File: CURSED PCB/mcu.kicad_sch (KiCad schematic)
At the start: 1 part, among them U3 STM32H733VGT6

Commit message: updated schematic
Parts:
- removed U3: STM32H733VGT6, stm:LQFP100_STM, symbol STM32H733VGT6:STM32H733VGT6
- added C2, C5: 6pF, Capacitor_SMD:C_0805_2012Metric_Pad1.18x1.45mm_HandSolder, symbol PCM_Capacitor_US_AKL:C_0201
- added C24: 10nF, Capacitor_SMD:C_0805_2012Metric_Pad1.18x1.45mm_HandSolder, symbol PCM_Capacitor_US_AKL:C_0201
- added C25, C26, C6: 100nF, Capacitor_SMD:C_0805_2012Metric_Pad1.18x1.45mm_HandSolder, symbol PCM_Capacitor_US_AKL:C_0201
- added C27: 4.7uF, Capacitor_SMD:C_0805_2012Metric_Pad1.18x1.45mm_HandSolder, symbol PCM_Capacitor_US_AKL:C_0201
- added C7: 1uF, Capacitor_SMD:C_0805_2012Metric_Pad1.18x1.45mm_HandSolder, symbol PCM_Capacitor_US_AKL:C_0201
- added D1: BLUE LED, LED_SMD:LED_1206_3216Metric_Pad1.42x1.75mm_HandSolder, symbol Device:LED
- added D2: RED LED, LED_SMD:LED_1206_3216Metric_Pad1.42x1.75mm_HandSolder, symbol Device:LED
- added J3: 2 Wire Block for laser, 691137710002:691137710002, symbol 691137710002:691137710002
- added JP1: Jumper, Jumper:SolderJumper-2_P1.3mm_Bridged2Bar_Pad1.0x1.5mm, symbol Jumper:Jumper_2_Small_Bridged
- added JP2: SolderJumper_2_Open, Jumper:SolderJumper-2_P1.3mm_Open_Pad1.0x1.5mm, symbol Jumper:SolderJumper_2_Open
- added R1, R2: 220R, Resistor_SMD:R_0805_2012Metric_Pad1.20x1.40mm_HandSolder, symbol Device:R_US
- added TP1: SCLK TP, TestPoint:TestPoint_Pad_1.5x1.5mm, symbol Connector:TestPoint
- added TP4: MOSI TP, TestPoint:TestPoint_Pad_1.5x1.5mm, symbol Connector:TestPoint
- added TP5: MISO TP, TestPoint:TestPoint_Pad_1.5x1.5mm, symbol Connector:TestPoint
- added U1: STM32G431KBT6, STM32G431KBT6:QFP80P900X900X160-32N, symbol STM32G431KBT6:STM32G431KBT6
- added U3: MIC94090YC6, Package_TO_SOT_SMD:SOT-363_SC-70-6, symbol Power_Management:MIC94090YC6
- added Y1: 24MHz crystal, Crystal:Crystal_SMD_Abracon_ABM8G-4Pin_3.2x2.5mm, symbol Device:Crystal_GND24
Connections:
- new net: D2.1 (K), R2.1
- new net: D1.2 (A), D2.2 (A), JP1.1 (A)
- new net: R2.2, U1.7 (PA2)
- new net: R1.2, U1.8 (PA3)
- new net: D1.1 (K), R1.1
- new net: J3.2, JP2.1 (A)
- new net: JP2.2 (B), U3.1 (OUT)
- new net +3.3VA: C24.2, C6.1, C7.2, U1.15 (VDDA/VREF+)
- new net +3.3VD: C25.2, C26.2, C27.2, JP1.2 (B), U1.1 (VDD), U1.17 (VDD)
- new net +5V: U3.4 (IN)
- new net CS2: U1.25 (PA15)
- new net CS_DAC: U1.13 (PB0)
- new net CUR_SEN: U1.5 (PA0)
- new net GND: C2.2, C24.1, C25.1, C26.1, C27.1, C5.2, C6.2, C7.1, J3.1, U1.14 (VSSA), U1.16 (VSS), U1.31 (PB8-BOOT0), U1.32 (VSS), U3.2 (GND), U3.5 (GND), Y1.2, Y1.4
- new net IRQ/MDAT: U1.6 (PA1)
- new net Las_enable: U1.30 (PB7), U3.6 (EN)
- new net MCLR: U1.4 (PG10-NRST)
- new net MISO: TP5.1, U1.11 (PA6)
- new net MKLKIN: U1.21 (PA11)
- new net MOSI: TP4.1, U1.12 (PA7)
- new net OCS1/CLKIN: C5.1, U1.2 (PF0-OSC_IN), Y1.3
- new net OCS2/CLKOUT: C2.1, U1.3 (PF1-OSC_OUT), Y1.1
- new net PGC: U1.23 (PA13)
- new net PGD: U1.24 (PA14)
- new net RXD: U1.20 (PA10)
- new net SCLK: TP1.1, U1.10 (PA5)
- new net TXD: U1.19 (PA9)
- no-connect marks 0 -> 6
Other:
- note added: "C5=C6=2*(C_L - C_S) C_L = 8 C_S = 5 C5=C6=6"

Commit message: updated schematic
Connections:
- net CS: now also U1.9 (PA4)
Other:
- note added: "Laser: https://www.iadiy.com/infrared-laser-module-LM9IR830H200D&path=168_173"
- moved on the sheet: C27, C7
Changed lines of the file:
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@@
 	(generator_version "9.0")
 	(paper "A4")
-	(text "C5=C6=2*(C_L - C_S)\n\nC_L = 8 \nC_S = 5\n\nC5=C6=6"
+	(text "Laser: https://www.iadiy.com/infrared-laser-module-LM9IR830H200D&path=168_173"
 		(exclude_from_sim no)
-		(at 31.75 151.13 0)
+		(at 225.298 159.512 0)
 		(effects
 			(font
@@
 		)
 	)
-	(junction
-		(at 191.77 58.42)
-		(diameter 0)
-		(color 0 0 0 0)
+	(text "C5=C6=2*(C_L - C_S)\n\nC_L = 8 \nC_S = 5\n\nC5=C6=6"
+		(exclude_from_sim no)
+		(at 37.338 137.414 0)
+		(effects
+			(font
+				(size 1.27 1.27)
+			)
+		)
 	)
 	(junction
@@
 	)
 	(junction
-		(at 189.23 58.42)
-		(diameter 0)
-		(color 0 0 0 0)
-	)
-	(junction
-		(at 191.77 49.53)
+		(at 193.04 49.53)
 		(diameter 0)
 		(color 0 0 0 0)
@@
 	)
 	(junction
-		(at 227.33 54.61)
+		(at 193.04 58.42)
 		(diameter 0)
 		(color 0 0 0 0)
 	)
 	(junction
-		(at 231.14 54.61)
+		(at 227.33 54.61)
 		(diameter 0)
 		(color 0 0 0 0)
@@
 	(wire
 		(pts
-			(xy 191.77 50.8) (xy 191.77 49.53)
+			(xy 193.04 50.8) (xy 193.04 49.53)
 		)
 		(stroke
@@
 	(wire
 		(pts
-			(xy 227.33 46.99) (xy 234.95 46.99)
+			(xy 193.04 58.42) (xy 200.66 58.42)
 		)
 		(stroke
@@
 	(wire
 		(pts
-			(xy 222.25 144.78) (xy 222.25 148.59)
+			(xy 227.33 46.99) (xy 233.68 46.99)
 		)
 		(stroke
@@
 	(wire
 		(pts
-			(xy 39.37 59.69) (xy 39.37 62.23)
+			(xy 222.25 144.78) (xy 222.25 148.59)
 		)
 		(stroke
@@
 	(wire
 		(pts
-			(xy 191.77 58.42) (xy 189.23 58.42)
+			(xy 39.37 59.69) (xy 39.37 62.23)
 		)
 		(stroke
@@
 	(wire
 		(pts
-			(xy 200.66 49.53) (xy 191.77 49.53)
+			(xy 200.66 49.53) (xy 193.04 49.53)
 		)
 		(stroke
@@
 	(wire
 		(pts
-			(xy 191.77 58.42) (xy 200.66 58.42)
-		)
-		(stroke
-			(width 0)
-			(type default)
-		)
-	)
-	(wire
-		(pts
 			(xy 91.44 85.09) (xy 109.22 85.09)
 		)
@@
 	(wire
 		(pts
-			(xy 189.23 58.42) (xy 189.23 62.23)
+			(xy 193.04 58.42) (xy 193.04 62.23)
 		)
 		(stroke
@@
 	(wire
 		(pts
-			(xy 231.14 54.61) (xy 234.95 54.61)
-		)
-		(stroke
-			(width 0)
-			(type default)
-		)
-	)
-	(wire
-		(pts
 			(xy 220.98 46.99) (xy 227.33 46.99)
 		)
@@
 	(wire
 		(pts
-			(xy 227.33 54.61) (xy 231.14 54.61)
+			(xy 227.33 54.61) (xy 233.68 54.61)
 		)
 		(stroke
@@
 	(wire
 		(pts
-			(xy 92.71 72.39) (xy 109.22 72.39)
+			(xy 77.47 74.93) (xy 85.09 74.93)
 		)
 		(stroke
@@
 	(wire
 		(pts
-			(xy 77.47 74.93) (xy 85.09 74.93)
+			(xy 71.12 137.16) (xy 71.12 142.24)
 		)
 		(stroke
@@
 	(wire
 		(pts
-			(xy 71.12 137.16) (xy 71.12 142.24)
+			(xy 91.44 72.39) (xy 109.22 72.39)
 		)
 		(stroke
@@
 	(wire
 		(pts
-			(xy 191.77 49.53) (xy 185.42 49.53)
+			(xy 185.42 49.53) (xy 193.04 49.53)
 		)
 		(stroke
@@
 	(wire
 		(pts
-			(xy 189.23 58.42) (xy 185.42 58.42)
+			(xy 185.42 58.42) (xy 193.04 58.42)
 		)
 		(stroke
@@
 	(wire
 		(pts
-			(xy 231.14 54.61) (xy 231.14 57.15)
+			(xy 227.33 54.61) (xy 227.33 57.15)
 		)
 		(stroke
@@
 	(symbol
 		(lib_id "PCM_Capacitor_US_AKL:C_0201")
-		(at 191.77 54.61 180)
+		(at 193.04 54.61 180)
 		(unit 1)
 		(exclude_from_sim no)
@@
 		(dnp no)
 		(property "Reference" "C7"
-			(at 194.818 53.34 0)
+			(at 196.088 53.34 0)
 			(effects
 				(font
@@
 		)
 		(property "Value" "1uF"
-			(at 194.818 55.88 0)
+			(at 196.088 55.88 0)
 			(effects
 				(font
@@
 		)
 		(property "Footprint" "Capacitor_SMD:C_0805_2012Metric_Pad1.18x1.45mm_HandSolder"
-			(at 190.8048 50.8 0)
+			(at 192.0748 50.8 0)
 			(effects
 				(font
@@
 		)
 		(property "Datasheet" "~"
-			(at 191.77 54.61 0)
+			(at 193.04 54.61 0)
 			(effects
 				(font
@@
 		)
 		(property "Description" "SMD 0201 MLCC capacitor, Alternate KiCad Library"
-			(at 191.77 54.61 0)
+			(at 193.04 54.61 0)
 			(effects
 				(font
@@
 	(symbol
 		(lib_id "power:GND")
-		(at 231.14 57.15 0)
+		(at 227.33 57.15 0)
 		(unit 1)
 		(exclude_from_sim no)
@@
 		(dnp no)
 		(property "Reference" "#PWR071"
-			(at 231.14 63.5 0)
+			(at 227.33 63.5 0)
 			(effects
 				(font
@@
 		)
 		(property "Value" "GND"
-			(at 231.1401 60.96 90)
+			(at 227.3301 60.96 90)
 			(effects
 				(font
@@
 		)
 		(property "Footprint" ""
-			(at 231.14 57.15 0)
+			(at 227.33 57.15 0)
 			(effects
 				(font
@@
 		)
 		(property "Datasheet" ""
-			(at 231.14 57.15 0)
+			(at 227.33 57.15 0)
 			(effects
 				(font
@@
 		)
 		(property "Description" "Power symbol creates a global label with name \"GND\" , ground"
-			(at 231.14 57.15 0)
+			(at 227.33 57.15 0)
 			(effects
 				(font
@@
 	(symbol
 		(lib_id "power:GND")
-		(at 189.23 62.23 0)
+		(at 193.04 62.23 0)
 		(unit 1)
 		(exclude_from_sim no)
@@
 		(dnp no)
 		(property "Reference" "#PWR068"
-			(at 189.23 68.58 0)
+			(at 193.04 68.58 0)
 			(effects
 				(font
@@
 		)
 		(property "Value" "GND"
-			(at 189.2301 66.04 90)
+			(at 193.0401 66.04 90)
 			(effects
 				(font
@@
 		)
 		(property "Footprint" ""
-			(at 189.23 62.23 0)
+			(at 193.04 62.23 0)
 			(effects
 				(font
@@
 		)
 		(property "Datasheet" ""
-			(at 189.23 62.23 0)
+			(at 193.04 62.23 0)
 			(effects
 				(font
@@
 		)
 		(property "Description" "Power symbol creates a global label with name \"GND\" , ground"
-			(at 189.23 62.23 0)
+			(at 193.04 62.23 0)
 			(effects
 				(font
@@
 	(symbol
 		(lib_id "PCM_Capacitor_US_AKL:C_0201")
-		(at 234.95 50.8 180)
+		(at 233.68 50.8 180)
 		(unit 1)
 		(exclude_from_sim no)
@@
 		(fields_autoplaced yes)
 		(property "Reference" "C27"
-			(at 238.76 49.5299 0)
+			(at 237.49 49.5299 0)
 			(effects
 				(font
@@
 		)
 		(property "Value" "4.7uF"
-			(at 238.76 52.0699 0)
+			(at 237.49 52.0699 0)
 			(effects
 				(font
@@
 		)
 		(property "Footprint" "Capacitor_SMD:C_0805_2012Metric_Pad1.18x1.45mm_HandSolder"
-			(at 233.9848 46.99 0)
+			(at 232.7148 46.99 0)
 			(effects
 				(font
@@
 		)
 		(property "Datasheet" "~"
-			(at 234.95 50.8 0)
+			(at 233.68 50.8 0)
 			(effects
 				(font
@@
 		)
 		(property "Description" "SMD 0201 MLCC capacitor, Alternate KiCad Library"
-			(at 234.95 50.8 0)
+			(at 233.68 50.8 0)
 			(effects
 				(font

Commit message: schematic changes
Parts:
- removed J3: 2 Wire Block for laser, 691137710002:691137710002, symbol 691137710002:691137710002
- added C35: 1uF, Capacitor_SMD:C_0805_2012Metric_Pad1.18x1.45mm_HandSolder, symbol PCM_Capacitor_US_AKL:C_0201
- added R15: 10K, Resistor_SMD:R_0805_2012Metric_Pad1.20x1.40mm_HandSolder, symbol Device:R_US
- renumbered TP5 to MITP1, TP4 to MOTP1, TP1 to SCTP1
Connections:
- net GND: now also C35.1, R15.1, R15.2
- net MCLR: now also C35.2
- net LASER: now reaches JP2.1 (A)

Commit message: schematic and layout changes
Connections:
- net DAC_RESET: now also U1.27 (PB4)
- no-connect marks 6 -> 5
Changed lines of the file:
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@@
 	)
 	(no_connect
-		(at 149.86 67.31)
-	)
-	(no_connect
 		(at 149.86 64.77)
 	)
@@
 	(wire
 		(pts
+			(xy 77.47 90.17) (xy 109.22 90.17)
+		)
+		(stroke
+			(width 0)
+			(type default)
+		)
+	)
+	(wire
+		(pts
 			(xy 74.93 137.16) (xy 71.12 137.16)
 		)
@@
 	(wire
 		(pts
-			(xy 91.44 85.09) (xy 109.22 85.09)
+			(xy 77.47 85.09) (xy 109.22 85.09)
 		)
 		(stroke
@@
 	(wire
 		(pts
-			(xy 91.44 87.63) (xy 109.22 87.63)
+			(xy 77.47 87.63) (xy 109.22 87.63)
 		)
 		(stroke
@@
 	(wire
 		(pts
-			(xy 88.9 97.79) (xy 109.22 97.79)
+			(xy 77.47 97.79) (xy 109.22 97.79)
 		)
 		(stroke
@@
 	(wire
 		(pts
-			(xy 88.9 100.33) (xy 109.22 100.33)
+			(xy 77.47 100.33) (xy 109.22 100.33)
 		)
 		(stroke
@@
 	(wire
 		(pts
-			(xy 91.44 90.17) (xy 109.22 90.17)
-		)
-		(stroke
-			(width 0)
-			(type default)
-		)
-	)
-	(wire
-		(pts
 			(xy 200.66 50.8) (xy 200.66 49.53)
 		)
@@
 	(wire
 		(pts
+			(xy 149.86 67.31) (xy 161.29 67.31)
+		)
+		(stroke
+			(width 0)
+			(type default)
+		)
+	)
+	(wire
+		(pts
 			(xy 81.28 64.77) (xy 109.22 64.77)
 		)
@@
 	(wire
 		(pts
-			(xy 88.9 95.25) (xy 109.22 95.25)
+			(xy 77.47 95.25) (xy 109.22 95.25)
 		)
 		(stroke
@@
 	(hierarchical_label "CS2"
 		(shape input)
-		(at 88.9 100.33 180)
+		(at 77.47 100.33 180)
 		(effects
 			(font
@@
 	(hierarchical_label "TXD"
 		(shape input)
-		(at 91.44 85.09 180)
+		(at 77.47 85.09 180)
 		(effects
 			(font
@@
 	(hierarchical_label "RXD"
 		(shape input)
-		(at 91.44 87.63 180)
+		(at 77.47 87.63 180)
 		(effects
 			(font
@@
 	(hierarchical_label "DAC_RESET"
 		(shape input)
-		(at 162.56 66.04 0)
+		(at 161.29 67.31 0)
 		(effects
 			(font
@@
 	(hierarchical_label "MKLKIN"
 		(shape input)
-		(at 91.44 90.17 180)
+		(at 77.47 90.17 180)
 		(effects
 			(font
@@
 	(hierarchical_label "PGC"
 		(shape input)
-		(at 88.9 95.25 180)
+		(at 77.47 95.25 180)
 		(effects
 			(font
@@
 	(hierarchical_label "PGD"
 		(shape input)
-		(at 88.9 97.79 180)
+		(at 77.47 97.79 180)
 		(effects
 			(font
@@
 		(dnp no)
 		(property "Reference" "MOTP1"
-			(at 83.058 80.772 0)
+			(at 64.008 80.518 0)
 			(effects
 				(font
@@
 		)
 		(property "Value" "MOSI TP"
-			(at 83.058 83.312 0)
+			(at 55.372 80.772 0)
 			(effects
 				(font
@@
 		(dnp no)
 		(property "Reference" "SCTP1"
-			(at 74.422 67.818 0)
+			(at 62.992 73.152 0)
 			(effects
 				(font
@@
 		)
 		(property "Value" "SCLK TP"
-			(at 74.422 70.358 0)
+			(at 53.34 73.152 0)
 			(effects
 				(font
@@
 		(dnp no)
 		(property "Reference" "MITP1"
-			(at 99.06 70.358 0)
+			(at 63.5 77.724 0)
 			(effects
 				(font
@@
 		)
 		(property "Value" "MISO TP"
-			(at 99.06 72.898 0)
+			(at 55.626 77.724 0)
 			(effects
 				(font

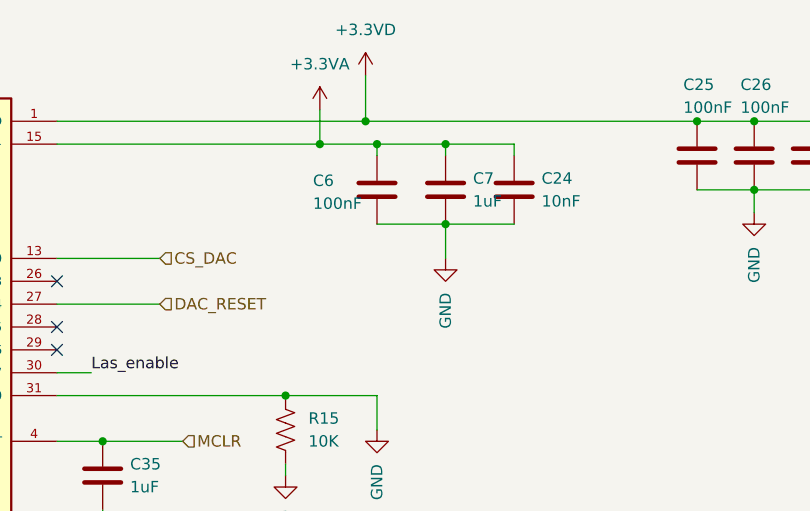
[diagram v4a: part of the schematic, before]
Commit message: updates traces and footprints
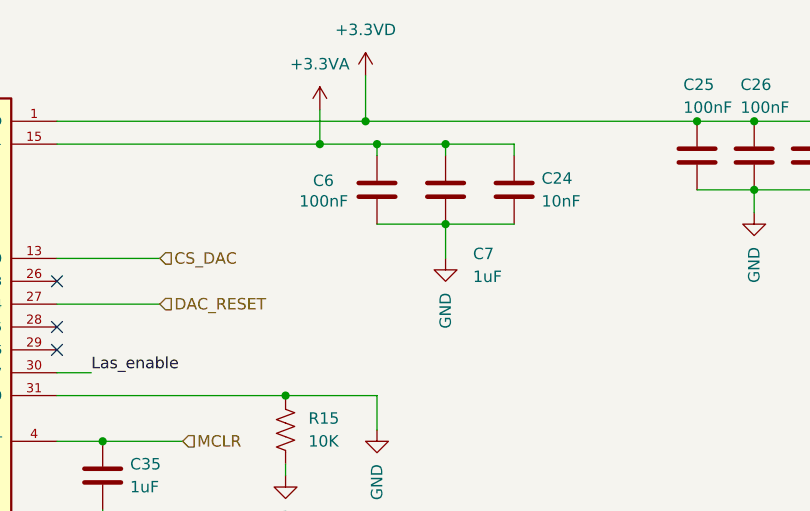
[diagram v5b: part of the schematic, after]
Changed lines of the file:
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@@
 		(dnp no)
 		(property "Reference" "C7"
-			(at 196.088 53.34 0)
+			(at 196.088 61.722 0)
 			(effects
 				(font
@@
 		)
 		(property "Value" "1uF"
-			(at 196.088 55.88 0)
+			(at 196.088 64.262 0)
 			(effects
 				(font
@@
 		)
 		(property "Value" "100nF"
-			(at 178.308 56.134 0)
-			(effects
-				(font
+			(at 176.784 55.88 0)
+			(effects
+				(font

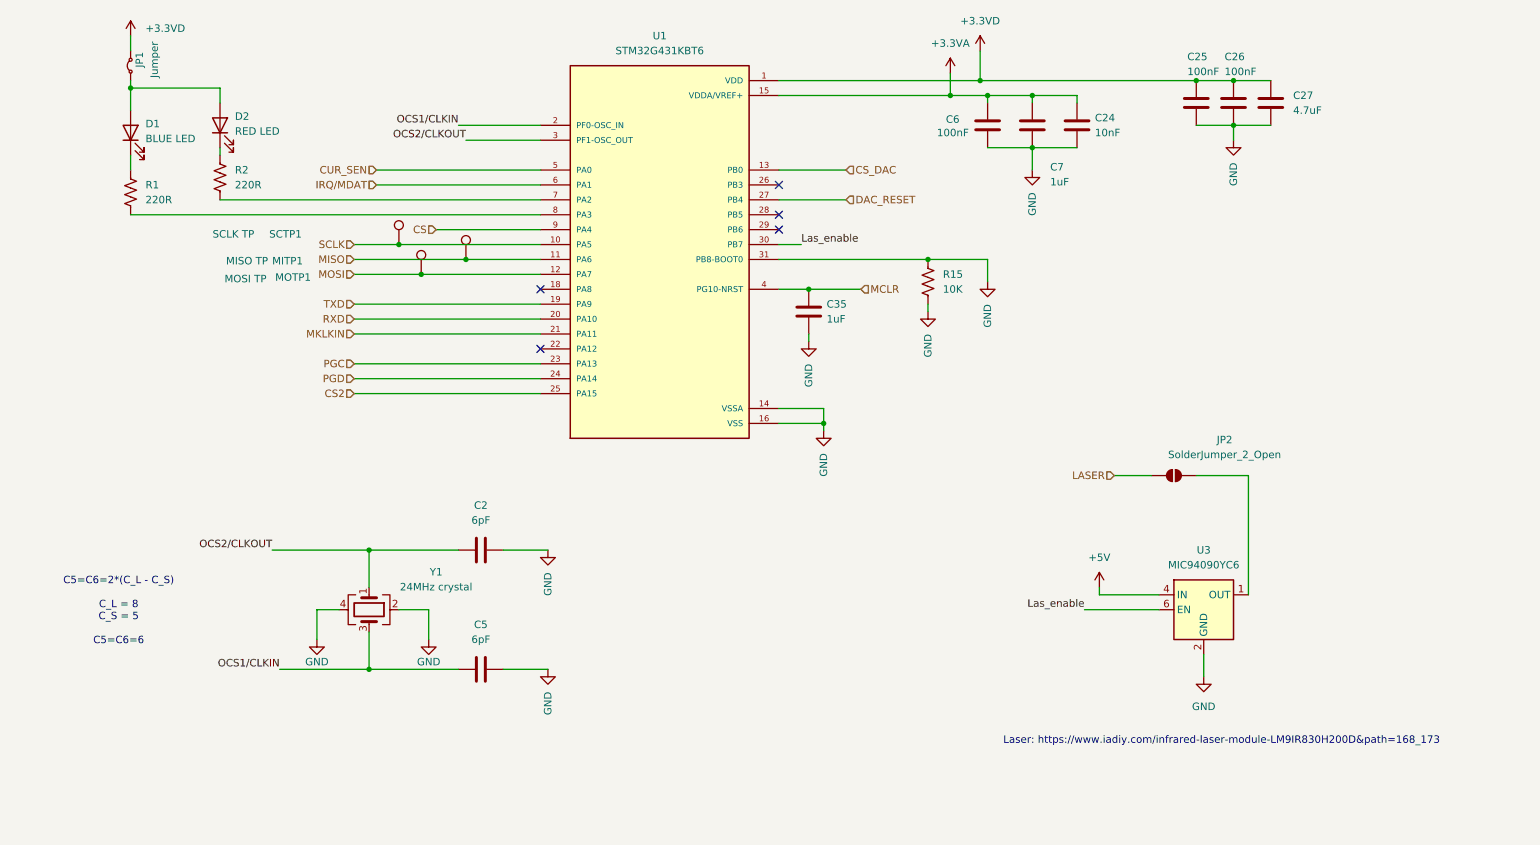
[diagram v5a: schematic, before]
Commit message: Updated PDF and make schematic look more pretty
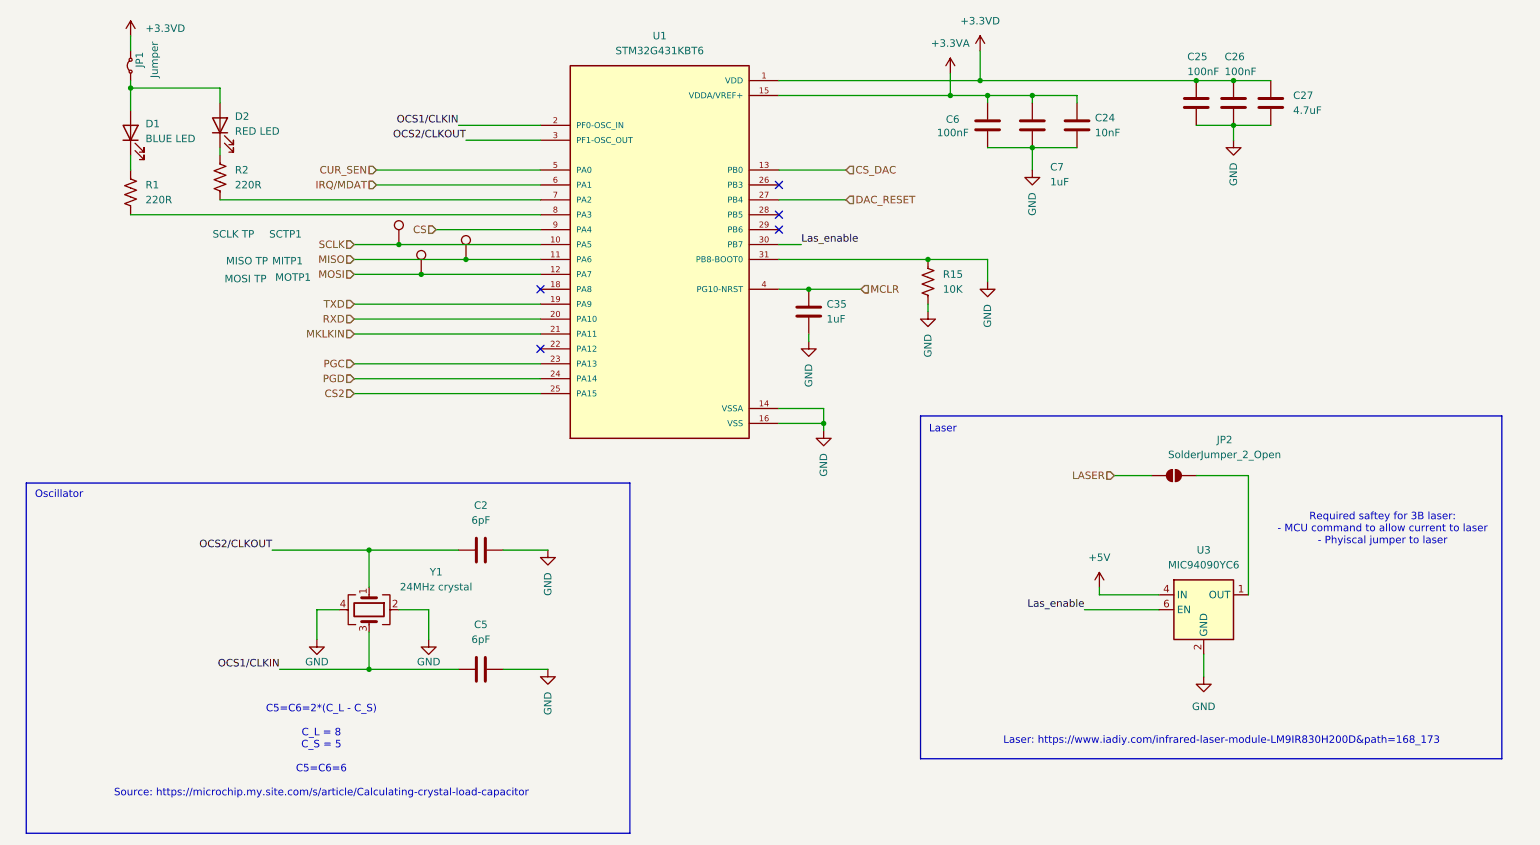
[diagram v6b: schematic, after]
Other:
- note added: "C5=C6=2*(C_L - C_S) C_L = 8 C_S = 5 C5=C6=6 Source: https://microchip.my.site.com/s/article/Calculating-crystal-load-capacitor"
- note added: "Laser"
- note added: "Oscillator"
- note added: "Required saftey for 3B laser: - MCU command to allow current to laser - Phyiscal jumper to laser"
- note removed: "C5=C6=2*(C_L - C_S) C_L = 8 C_S = 5 C5=C6=6"
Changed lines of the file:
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@@
 	(generator_version "9.0")
 	(paper "A4")
+	(rectangle
+		(start 173.99 104.14)
+		(end 273.05 162.56)
+		(stroke
+			(width 0)
+			(type default)
+		)
+		(fill
+			(type none)
+		)
+	)
+	(rectangle
+		(start 21.59 115.57)
+		(end 124.46 175.26)
+		(stroke
+			(width 0)
+			(type default)
+		)
+		(fill
+			(type none)
+		)
+	)
 	(text "Laser: https://www.iadiy.com/infrared-laser-module-LM9IR830H200D&path=168_173"
 		(exclude_from_sim no)
@@
 		)
 	)
-	(text "C5=C6=2*(C_L - C_S)\n\nC_L = 8 \nC_S = 5\n\nC5=C6=6"
+	(text "Laser"
 		(exclude_from_sim no)
-		(at 37.338 137.414 0)
+		(at 177.8 106.426 0)
 		(effects
 			(font
+				(size 1.27 1.27)
+			)
+		)
+	)
+	(text "Oscillator"
+		(exclude_from_sim no)
+		(at 27.178 117.602 0)
+		(effects
+			(font
+				(size 1.27 1.27)
+			)
+		)
+	)
+	(text "C5=C6=2*(C_L - C_S)\n\nC_L = 8 \nC_S = 5\n\nC5=C6=6\n\nSource: https://microchip.my.site.com/s/article/Calculating-crystal-load-capacitor"
+		(exclude_from_sim no)
+		(at 71.882 161.29 0)
+		(effects
+			(font
+				(size 1.27 1.27)
+			)
+		)
+	)
+	(text "Required saftey for 3B laser:\n- MCU command to allow current to laser\n- Phyiscal jumper to laser"
+		(exclude_from_sim no)
+		(at 252.73 123.444 0)
+		(effects
+			(font
